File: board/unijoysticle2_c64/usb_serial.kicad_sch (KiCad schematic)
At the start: 12 parts, among them J1 USB_B_Micro, U2 AMS1117-3.3, U3 CH340C

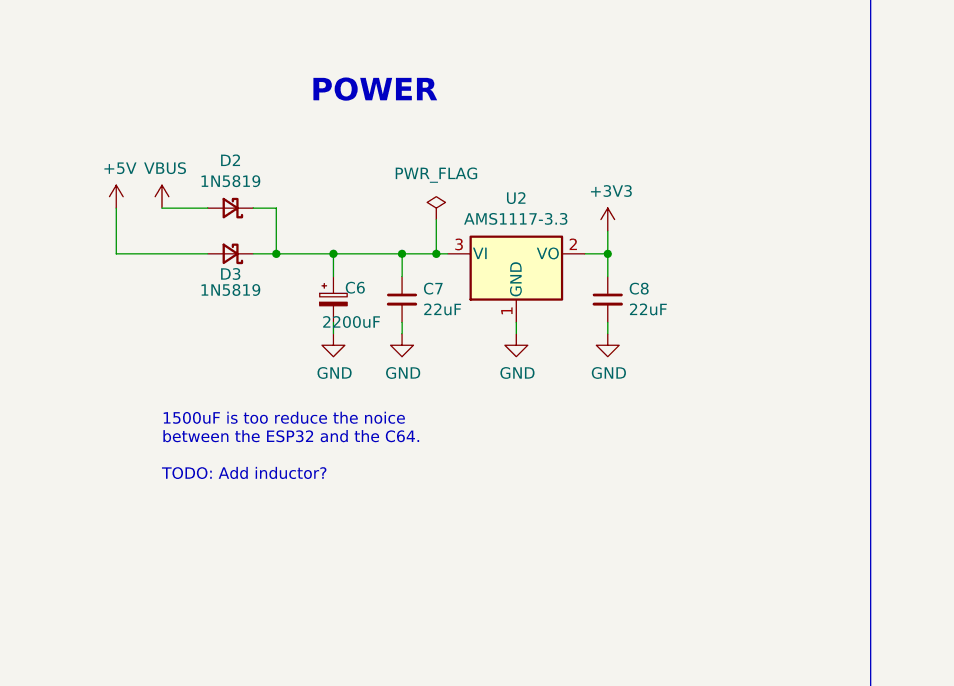
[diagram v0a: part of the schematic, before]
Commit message: c64: back to using SMD cap for 2200uf
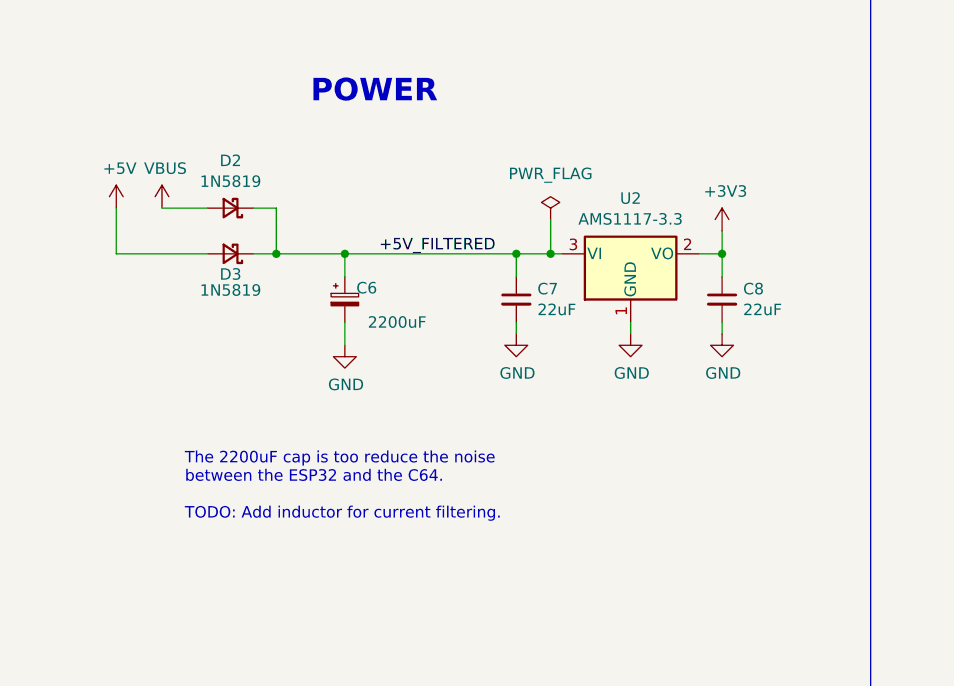
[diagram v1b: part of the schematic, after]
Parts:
- C6: footprint Capacitor_THT:CP_Radial_D10.0mm_P5.00mm -> Capacitor_SMD:CP_Elec_10x10.5
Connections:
- net +5V_FILTERED: now reaches C6.1, C7.1, D2.1 (K), D3.1 (K), U2.3 (VI)
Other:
- note added: "The 2200uF cap is too reduce the noise between the ESP32 and the C64. TODO: Add inductor for current filtering."
- note removed: "1500uF is too reduce the noice between the ESP32 and the C64. TODO: Add inductor?"
- moved on the sheet: C6, C7, C8, U2

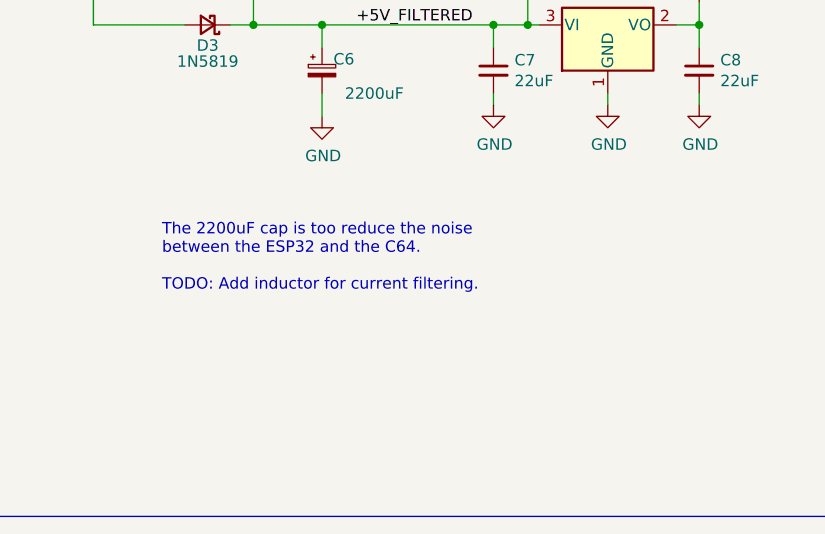
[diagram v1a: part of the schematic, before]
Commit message: c64: layout improvements
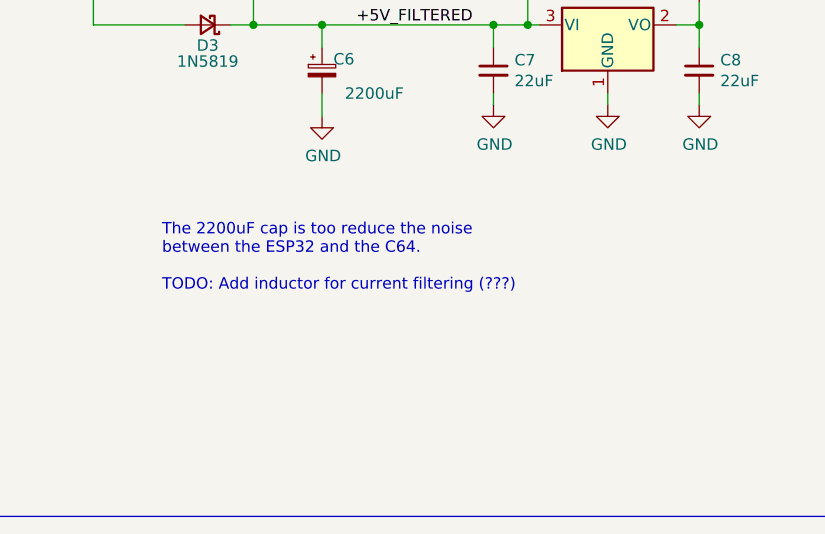
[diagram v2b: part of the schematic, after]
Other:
- note added: "The 2200uF cap is too reduce the noise between the ESP32 and the C64. TODO: Add inductor for current filtering (???)"
- note removed: "The 2200uF cap is too reduce the noise between the ESP32 and the C64. TODO: Add inductor for current filtering."
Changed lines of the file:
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@@
     (effects (font (size 2 2)) (justify left bottom))
   )
-  (text "The 2200uF cap is too reduce the noise\nbetween the ESP32 and the C64.\n\nTODO: Add inductor for current filtering.\n\n"
+  (text "The 2200uF cap is too reduce the noise\nbetween the ESP32 and the C64.\n\nTODO: Add inductor for current filtering (???)\n\n"
     (at 36.83 80.01 0)
     (effects (font (size 1.27 1.27)) (justify left bottom))

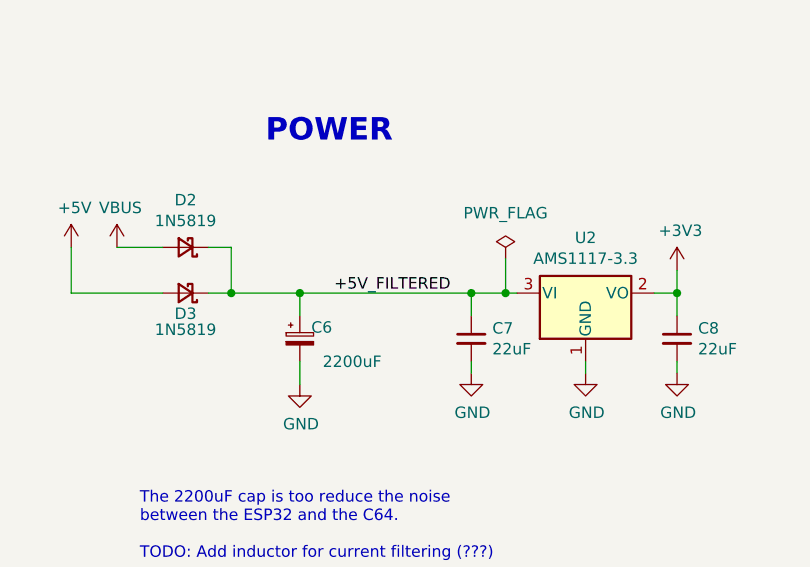
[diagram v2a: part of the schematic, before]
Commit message: c64: more progress on routing
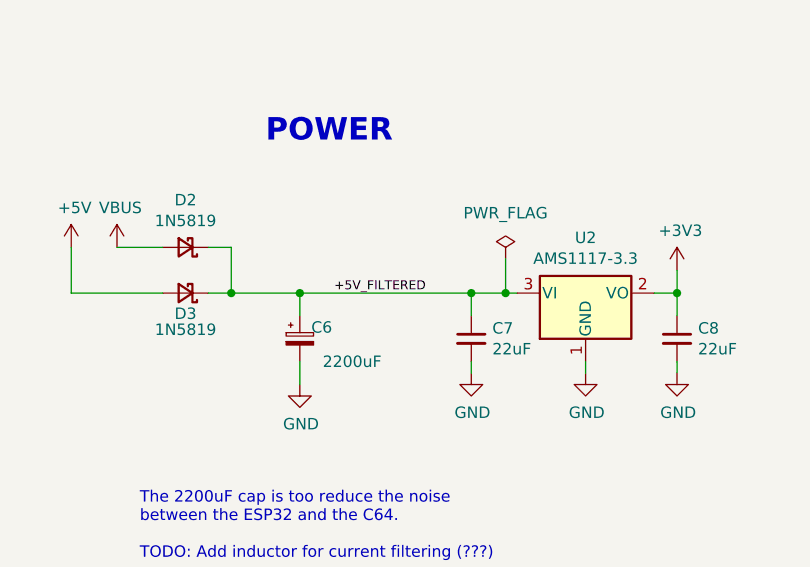
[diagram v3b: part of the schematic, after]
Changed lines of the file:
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@@
   )
   (label "+5V_FILTERED" (at 58.42 48.26 0)
-    (effects (font (size 1.27 1.27)) (justify left bottom))
+    (effects (font (size 1 1)) (justify left bottom))
   )
   (global_label "RTS_PROG" (shape input) (at 210.82 59.69 0) (fields_autoplaced)
